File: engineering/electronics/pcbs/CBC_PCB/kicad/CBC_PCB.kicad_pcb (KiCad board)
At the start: 6 copper layers, 178 x 211 mm, 212 parts, among them J2 AT13-12PB-BM03, J4 AMT0650009DB0000G, J5 AMT0650009DB0000G, J6 AMT0650009DB0000G, J7 AMT0650009DB0000G, Q4 SP015N03BGHTO, U10 CPC1106NTR, U11 CPC1106NTR, U12 74LVC1G17W5-7, U13 74LVC2G02HK3-7, U14 MAX810R, U15 XL7056E1, U16 1kΩ, U17 1kΩ, U18 1kΩ, U19 1kΩ, U2 2.4GHz, U20 1kΩ, U21 1kΩ, U22 CPC1019NTR, U23 MP9486GN-Z, U25 ADM3053BRWZ-REEL7, U26 ADM3053BRWZ-REEL7, U27 10mΩ, U29 1uF, U30 1uH, U31 1kΩ, U32 1kΩ, U4 1kΩ, U9 120pF, X1 8MHz, X2 8MHz

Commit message: electronics: integrate CBC PCB updates
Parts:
- removed C29, C34: 100uF, EasyEDA_Lib:CAP-TH_BD10.0-P5.00-D1.0-FD
- removed C30, C32, C33: 100nF, EasyEDA_Lib:C0603
- removed L3: 100uH, EasyEDA_Lib:IND-SMD_L7.1-W6.6
- added C100: 100nF, EasyEDA_Lib:C0603, F.Cu at (106.0, 115.0)
- added C101: 100nF, EasyEDA_Lib:C0603, F.Cu at (109.2, 136.6)
- added C102: 10uF, EasyEDA_Lib:CAP-SMD_L3.5-W2.8-R-RD, F.Cu at (112.2, 135.4)
- added C103: 100nF, EasyEDA_Lib:C0603, F.Cu at (92.3, 137.6)
- added C104: 10uF, EasyEDA_Lib:CAP-SMD_L3.5-W2.8-R-RD, F.Cu at (95.3, 136.4)
- added C105: 4.7uF, EasyEDA_Lib:C0805, F.Cu at (183.6, 190.0)
- added C106: 4.7uF, EasyEDA_Lib:C0805, F.Cu at (183.6, 192.2)
- added C107: 100nF, EasyEDA_Lib:C0603, F.Cu at (183.6, 194.5)
- added C36: 100nF, EasyEDA_Lib:C0603, F.Cu at (194.5, 226.9)
- added C78: 2.2uF, EasyEDA_Lib:CAP-TH_BD5.0-P2.00-D0.5-FD-1, F.Cu at (218.3, 216.8)
- added C79: 2.2uF, EasyEDA_Lib:CAP-TH_BD5.0-P2.00-D0.5-FD-1, F.Cu at (224.3, 216.8)
- added C80: 100nF, EasyEDA_Lib:C0603, F.Cu at (209.3, 214.3)
- added C81: 4.7uF, EasyEDA_Lib:C0805, F.Cu at (188.6, 222.5)
- added C82: 4.7uF, EasyEDA_Lib:C0805, F.Cu at (188.6, 225.4)
- added C83: 4.7uF, EasyEDA_Lib:C0805, F.Cu at (188.6, 228.4)
- added C84: 100nF, EasyEDA_Lib:C0603, F.Cu at (204.1, 219.6)
- added C85: 2.2uF, EasyEDA_Lib:CAP-TH_BD5.0-P2.00-D0.5-FD-1, F.Cu at (218.3, 184.3)
- added C86: 2.2uF, EasyEDA_Lib:CAP-TH_BD5.0-P2.00-D0.5-FD-1, F.Cu at (224.9, 184.3)
- added C87: 100nF, EasyEDA_Lib:C0603, F.Cu at (209.2, 181.7)
- added C88: 100nF, EasyEDA_Lib:C0603, F.Cu at (194.5, 194.5)
- added C89: 4.7uF, EasyEDA_Lib:C0805, F.Cu at (188.6, 190.0)
- added C90: 4.7uF, EasyEDA_Lib:C0805, F.Cu at (188.6, 192.9)
- added C91: 4.7uF, EasyEDA_Lib:C0805, F.Cu at (188.6, 195.9)
- added C92: 100nF, EasyEDA_Lib:C0603, F.Cu at (203.8, 187.2)
- added C93: 2.2uF, EasyEDA_Lib:CAP-TH_BD5.0-P2.00-D0.5-FD-1, F.Cu at (99.0, 101.7)
- added C94: 2.2uF, EasyEDA_Lib:CAP-TH_BD5.0-P2.00-D0.5-FD-1, F.Cu at (106.5, 101.7)
- added C95: 100nF, EasyEDA_Lib:C0603, F.Cu at (100.3, 110.2)
- added C96: 100nF, EasyEDA_Lib:C0603, F.Cu at (112.6, 123.5)
- added C97: 4.7uF, EasyEDA_Lib:C0805, F.Cu at (107.7, 128.5)
- added C98: 4.7uF, EasyEDA_Lib:C0805, F.Cu at (101.8, 128.5)
- added C99: 4.7uF, EasyEDA_Lib:C0805, F.Cu at (107.7, 130.9)
- added D24: ~, EasyEDA_Lib:TO-277A_L5.9-W4.4-LS6.5-TR, F.Cu at (212.5, 209.0)
- added D25: ~, EasyEDA_Lib:SMB_L4.6-W3.6-LS5.3-BI, F.Cu at (206.9, 227.1)
- added D26: ~, EasyEDA_Lib:TO-277A_L5.9-W4.4-LS6.5-TR, F.Cu at (212.5, 176.5)
- added D27: ~, EasyEDA_Lib:SMB_L4.6-W3.6-LS5.3-BI, F.Cu at (206.7, 195.1)
- added D28: ~, EasyEDA_Lib:TO-277A_L5.9-W4.4-LS6.5-TR, F.Cu at (96.2, 109.0)
- added D29: ~, EasyEDA_Lib:SMB_L4.6-W3.6-LS5.3-BI, F.Cu at (113.9, 112.6)
- added D30: SS34, Diode_SMD:D_SMA, F.Cu at (187.6, 184.5)
- added L7: 33uH, EasyEDA_Lib:IND-SMD_L8.5-W8.0_SMS0850, F.Cu at (197.2, 217.1)
- added L8: 33uH, EasyEDA_Lib:IND-SMD_L8.5-W8.0_SMS0850, F.Cu at (197.0, 184.5)
- added L9: 33uH, EasyEDA_Lib:IND-SMD_L8.5-W8.0_SMS0850, F.Cu at (102.8, 121.5)
- added R49: 590K, 0603, EasyEDA_Lib:R0603, F.Cu at (194.5, 224.7)
- added R50: 10kΩ, EasyEDA_Lib:R0603, F.Cu at (197.9, 224.7)
- added R51: 140kΩ, EasyEDA_Lib:R0603, F.Cu at (210.0, 223.4)
- added R52: 10kΩ, EasyEDA_Lib:R0603, F.Cu at (206.6, 223.4)
- added R53: 10Ω, EasyEDA_Lib:R2512, F.Cu at (219.4, 191.0)
- added R54: 590K, 0603, EasyEDA_Lib:R0603, F.Cu at (194.5, 192.2)
- added R55: 10kΩ, EasyEDA_Lib:R0603, F.Cu at (198.0, 192.2)
- added R56: 140kΩ, EasyEDA_Lib:R0603, F.Cu at (210.0, 191.1)
- added R57: 10kΩ, EasyEDA_Lib:R0603, F.Cu at (206.5, 191.1)
- added R58: 240kΩ, EasyEDA_Lib:R0603, F.Cu at (110.6, 120.2)
- added R59: 10kΩ, EasyEDA_Lib:R0603, F.Cu at (110.6, 123.5)
- added R60: 140kΩ, EasyEDA_Lib:R0603, F.Cu at (110.6, 107.5)
- added R61: 10kΩ, EasyEDA_Lib:R0603, F.Cu at (110.6, 111.0)
- added R62: 100Ω, EasyEDA_Lib:R0603, F.Cu at (103.0, 141.3)
- added U33: MP9486GN-Z, CBC_PCB:SOIC-8EP_MP9486_MNP, F.Cu at (209.3, 219.0)
- added U34: MP9486GN-Z, CBC_PCB:SOIC-8EP_MP9486_MNP, F.Cu at (209.3, 186.5)
- added U35: MP9486GN-Z, CBC_PCB:SOIC-8EP_MP9486_MNP, F.Cu at (104.7, 110.2)
- added U36: ~, EasyEDA_Lib:SOT-223-3_L6.5-W3.4-P2.30-LS7.0-BR, F.Cu at (103.4, 135.9)
- added U37: MAX40203AUK+T, EasyEDA_Lib:MAX40203AUK_T_SOT-23-5, F.Cu at (95.8, 126.4)
- added U38: MAX40203AUK+T, EasyEDA_Lib:MAX40203AUK_T_SOT-23-5, F.Cu at (75.2, 141.9)
- added U39: MAX40203AUK+T, EasyEDA_Lib:MAX40203AUK_T_SOT-23-5, F.Cu at (106.0, 142.0)
- D5: value ~ -> SS34; footprint EasyEDA_Lib:TO-277A_L5.9-W4.4-LS6.5-TR -> Diode_SMD:D_SMA
- R17: value 2.7kΩ -> 100Ω
- R18: value 23.7kΩ -> 100Ω
- R19: value 60mΩ -> 100Ω; footprint EasyEDA_Lib:R1206 -> EasyEDA_Lib:R0603
- U15: value XL7056E1 -> MAX40203AUK+T; footprint EasyEDA_Lib:TO-263-7_L9.3-W10.0-P1.27-LB-LS15.0 -> EasyEDA_Lib:MAX40203AUK_T_SOT-23-5
- moved R17 241.7 mm to (65.1, 122.3), turned to 180 degrees
- moved U15 238.2 mm to (65.1, 126.4), turned to 180 degrees
- moved R19 212.5 mm to (72.3, 141.2), turned to 90 degrees
- moved R18 210.8 mm to (95.8, 122.3)
- moved R29 208.5 mm to (127.7, 55.6), turned to 180 degrees
- moved U10 203.9 mm to (132.9, 49.5)
- moved R15 203.0 mm to (128.4, 49.9)
- moved U22 202.9 mm to (132.9, 56.9), turned to -90 degrees
- moved R16 202.1 mm to (140.5, 51.8)
- moved U13 202.1 mm to (139.6, 54.0)
- moved U14 202.1 mm to (140.1, 57.6)
- moved C31 202.1 mm to (142.2, 53.4)
- moved C68 173.7 mm to (141.9, 202.2), turned to 0 degrees
- moved U27 168.3 mm to (126.2, 160.0), turned to -90 degrees
- moved D21 168.1 mm to (136.9, 186.5)
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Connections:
- net DATA1 renamed TEMP1_DQ
- net DATA2 renamed TEMP2_DQ
- C35 pad 2: +5V -> +5V_P1
- C38 pad 2: +5V -> +5V_P1
- C40 pad 2: +5V -> +5V_P1
- C45 pad 1: +3V3 -> +3V3_P1
- C46 pad 1: +3V3 -> +3V3_P1
- C74 pad 2: +5V -> +5V_P1
- D5 pad 1: H_PWR-IN- -> 12V_GATE_V
- D5 pad 2: H_PWR-IN- -> 12V_GATE_P1
- L4 pad 2: +5V -> +5V_P1
- R17 pad 1: H_PWR-IN- -> +5V_P1
- R17 pad 2: Net-(U15-FB) -> Net-(U15-EN)
- R18 pad 1: Net-(U15-FB) -> +5V_P2
- R18 pad 2: 12V_GATE_V -> Net-(U37-EN)
- R19 pad 1: Net-(U15-CSN) -> +3V3_P1
- R19 pad 2: 12V_GATE_V -> Net-(U38-EN)
- R31 pad 2: +5V -> +5V_P1
- R48 pad 1: Net-(U15-VIN) -> Net-(U33-VIN)
- U15 pad 1: H_PWR-IN- -> +5V_P1
- U15 pad 2: Net-(U15-FB) -> GND
- U15 pad 3: Net-(U15-CSN) -> Net-(U15-EN)
- U15 pad 4: Net-(D5-K) -> unconnected-(U15-NC-Pad4)
- U15 pad 5: 12V_GATE_V -> +5V
- U24 pad 2: +3V3 -> +3V3_P1
- U24 pad 4: +3V3 -> +3V3_P1
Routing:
- net H_PWR-IN: track 15.1 -> 87.1 mm
- net Net-(U15-CSN): track 50.0 -> 0.00 mm
- net +3V3: track 269.1 -> 229.6 mm, vias 11 -> 9
- net +5V: track 139.5 -> 107.2 mm, vias 4 -> 3
- net 12V_GATE_V: track 33.2 -> 1.59 mm, vias 4 -> 1
- net Net-(D18-A): track 2.34 -> 32.7 mm, vias 1 -> 0
- net +5V_P1: track 0.00 -> 29.1 mm, vias 0 -> 1
- net GND: track 191.4 -> 169.6 mm, vias 78 -> 77
- net +3V3_P1: track 0.00 -> 20.7 mm
- net Net-(D5-K): track 18.2 -> 0.00 mm
- net Net-(U15-FB): track 14.8 -> 0.00 mm
- net Net-(D16-A): track 0.00 -> 12.4 mm
- net /POWER SECTION/MOSFET_CONTROL_SIGNAL: track 11.0 -> 0.00 mm
- net H_PWR-IN-: track 8.65 -> 0.00 mm
- net Net-(U11-Load-Pad3): track 8.47 -> 0.00 mm, vias 1 -> 0
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- added copper zone on B.Cu, net Net-(C66-Pad2)
- added copper zone on F.Cu, net Net-(C66-Pad2)
- added copper zone on In1.Cu, net Net-(C66-Pad2)
- added copper zone on In4.Cu, net Net-(C66-Pad2)
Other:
- outline, holes or cut-outs redrawn

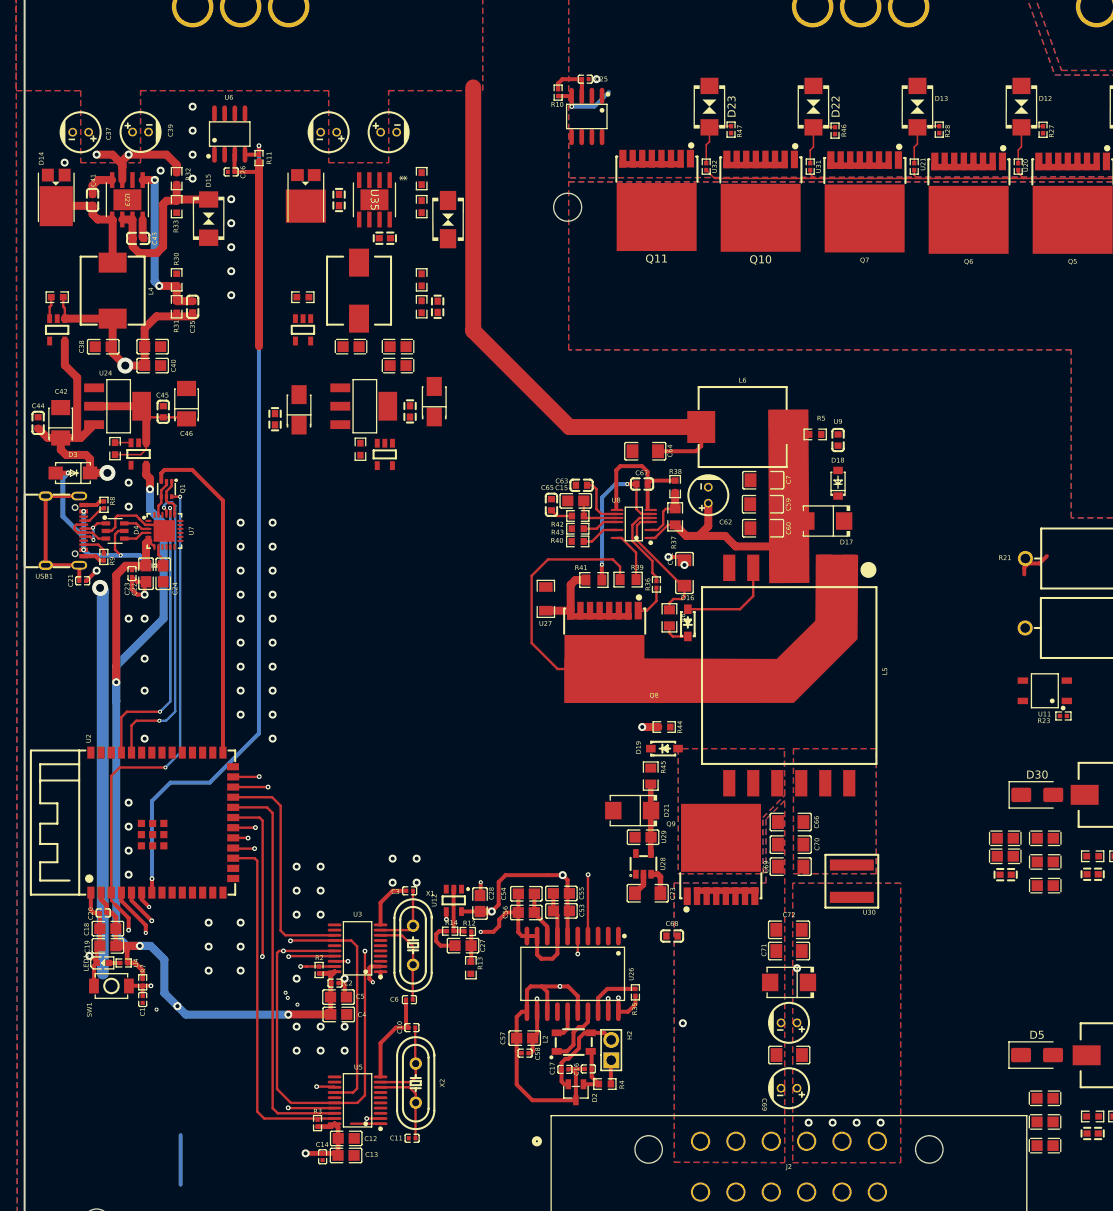
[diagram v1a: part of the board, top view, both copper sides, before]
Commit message: electronics: update CBC PCB and crystal parts
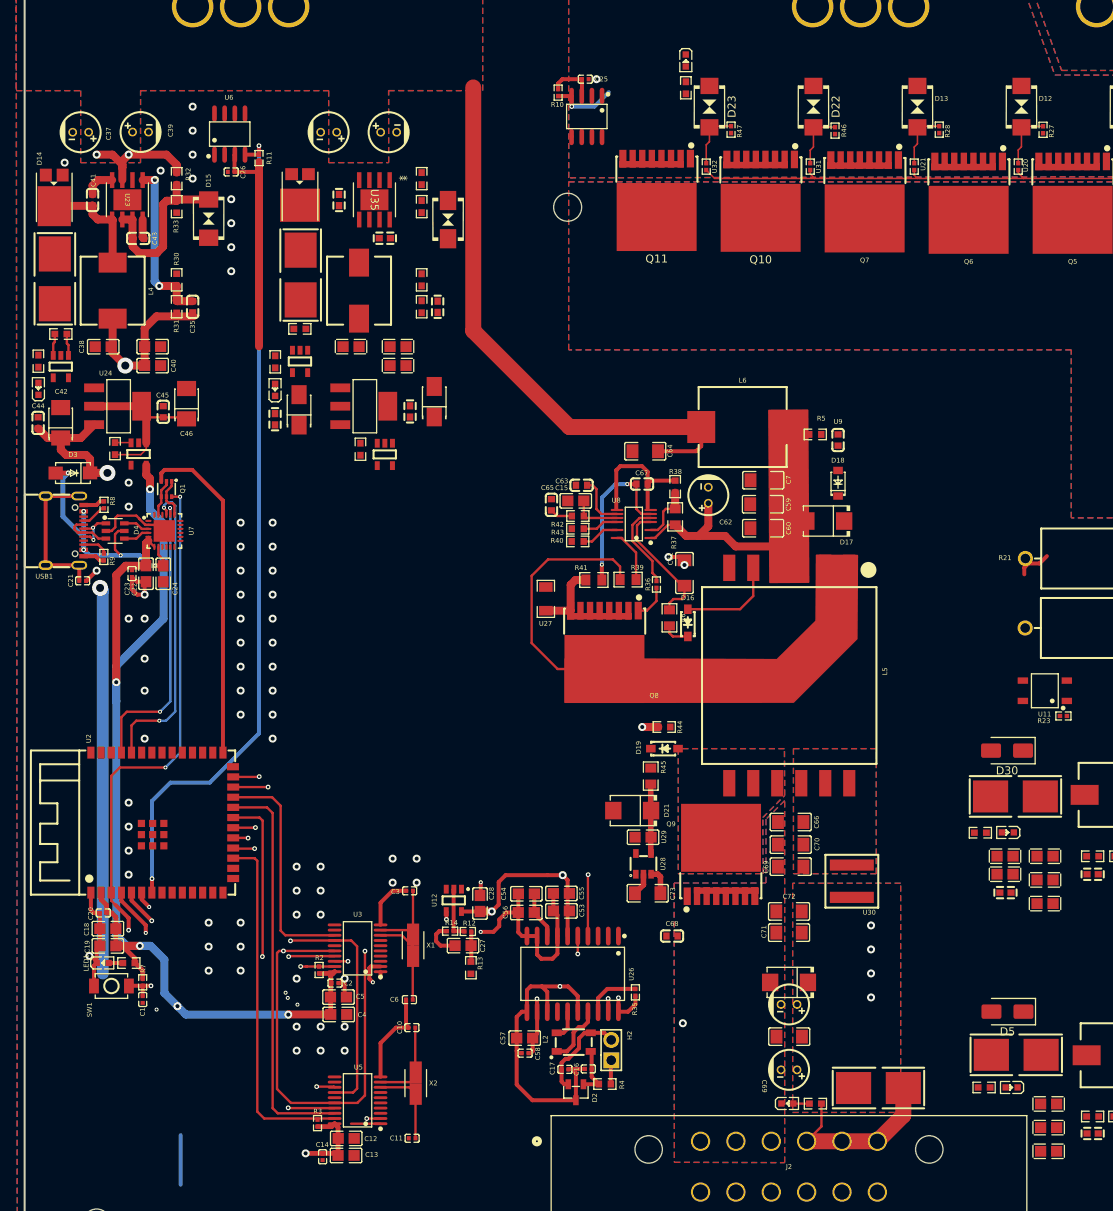
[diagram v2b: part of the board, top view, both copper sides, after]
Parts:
- removed U4: 1kΩ, EasyEDA_Lib:R0402
- added F2: ~, EasyEDA_Lib:FUSE-SMD_L9.8-W5.1, F.Cu at (184.9, 217.0)
- added F3: ~, EasyEDA_Lib:FUSE-SMD_L9.8-W5.1, F.Cu at (184.8, 184.7)
- added F4: ~, EasyEDA_Lib:FUSE-SMD_L9.8-W5.1, F.Cu at (64.8, 120.0)
- added F5: ~, EasyEDA_Lib:FUSE-SMD_L9.8-W5.1, F.Cu at (95.5, 119.5)
- added F6: 0154005.DR, EasyEDA_Lib:FUSE-SMD_L9.8-W5.1, F.Cu at (167.7, 221.2)
- added LED2: ~, EasyEDA_Lib:LED0603-RD, F.Cu at (184.4, 221.1)
- added LED3: ~, EasyEDA_Lib:LED0603-RD, F.Cu at (183.9, 189.2)
- added LED4: ~, EasyEDA_Lib:LED0603-RD, F.Cu at (143.6, 92.7)
- added LED5: ~, EasyEDA_Lib:LED0603-RD, F.Cu at (62.7, 133.8)
- added LED6: ~, EasyEDA_Lib:LED0603-RD, F.Cu at (92.3, 133.9)
- added LED7: ~, EasyEDA_Lib:LED0603-RD, F.Cu at (156.3, 223.1)
- added R63: 1.8kΩ, EasyEDA_Lib:R0603, F.Cu at (180.9, 221.1)
- added R64: 1.8kΩ, EasyEDA_Lib:R0603, F.Cu at (180.5, 189.3)
- added R65: 1.8kΩ, EasyEDA_Lib:R0603, F.Cu at (143.7, 96.1)
- added R66: 390Ω, EasyEDA_Lib:R0603, F.Cu at (62.7, 130.3)
- added R67: 390Ω, EasyEDA_Lib:R0603, F.Cu at (92.3, 130.4)
- added R68: 1.8kΩ, EasyEDA_Lib:R0603, F.Cu at (159.8, 223.1)
- added R69: 39Ω, EasyEDA_Lib:R0603, F.Cu at (74.0, 205.6)
- X1, X2: value 8MHz -> 16MHz; footprint EasyEDA_Lib:HC-49S_L11.5-W4.7-P4.88 -> EasyEDA_Lib:CRYSTAL-SMD_L3.2-W2.5_3225-8MHZ
- moved D30 6.70 mm to (183.8, 179.0), turned to 180 degrees
- moved D5 6.57 mm to (183.8, 211.6), turned to 180 degrees
- moved U15 4.62 mm to (65.5, 131.0)
- moved R17 4.62 mm to (65.5, 126.9)
- moved R18 3.97 mm to (95.4, 126.3)
- moved U37 3.97 mm to (95.4, 130.4)
- moved C71 2.30 mm to (156.6, 201.8)
- moved C72 2.30 mm to (156.6, 199.1)
- moved C75 2.30 mm to (156.6, 210.7)
- moved C77 2.30 mm to (156.6, 214.8)
- moved C76 2.30 mm to (156.6, 218.9)
- moved C107 2.24 mm to (183.6, 196.8)
- moved C105 2.24 mm to (183.6, 192.2)
- moved C106 2.24 mm to (183.6, 194.4)
- moved C89 2.24 mm to (188.6, 192.2)
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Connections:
- C71 pad 2: 12V_ISOLATED -> Net-(C71-Pad2)
- C72 pad 2: 12V_ISOLATED -> Net-(C71-Pad2)
- C75 pad 1: 12V_ISOLATED -> Net-(C71-Pad2)
- C76 pad 1: 12V_ISOLATED -> Net-(C71-Pad2)
- C77 pad 2: 12V_ISOLATED -> Net-(C71-Pad2)
- D20 pad 1: 12V_ISOLATED -> Net-(C71-Pad2)
- D30 pad 2: 12V_GATE_P2 -> Net-(D30-A)
- D5 pad 2: 12V_GATE_P1 -> Net-(D5-A)
- R17 pad 1: +5V_P1 -> Net-(U15-VDD)
- R18 pad 1: +5V_P2 -> Net-(U37-VDD)
- U15 pad 1: +5V_P1 -> Net-(U15-VDD)
- U30 pad 2: 12V_ISOLATED -> Net-(C71-Pad2)
- U37 pad 1: +5V_P2 -> Net-(U37-VDD)
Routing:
- net 12V_ISOLATED: track 0.00 -> 22.3 mm, vias 5 -> 0
- net +5V: track 107.2 -> 94.4 mm
- net +5V_P1: track 29.1 -> 20.3 mm
- net Net-(U15-VDD): track 0.00 -> 2.76 mm
- net Net-(LED7-A): track 0.00 -> 2.01 mm
- net +3V3: track 229.6 -> 229.0 mm
- net Net-(C71-Pad2): vias 0 -> 4
- net GND: vias 77 -> 76
- added copper zone on B.Cu, net Net-(C71-Pad2)
- added copper zone on F.Cu, net Net-(C71-Pad2)
- added copper zone on In1.Cu, net Net-(C71-Pad2)
- added copper zone on In4.Cu, net Net-(C71-Pad2)
- removed copper zone on B.Cu, net 12V_ISOLATED
- removed copper zone on F.Cu, net 12V_ISOLATED
- removed copper zone on In1.Cu, net 12V_ISOLATED
- removed copper zone on In4.Cu, net 12V_ISOLATED
